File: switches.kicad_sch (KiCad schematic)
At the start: 31 parts, among them J5 BM07B-SRSS-TB, SW1 B3FS-1052, SW2 291V1022F832AB, SW3 PEC164220F-S0024, SW4 MS-22C01-G010, U4 MCP23S17_ML

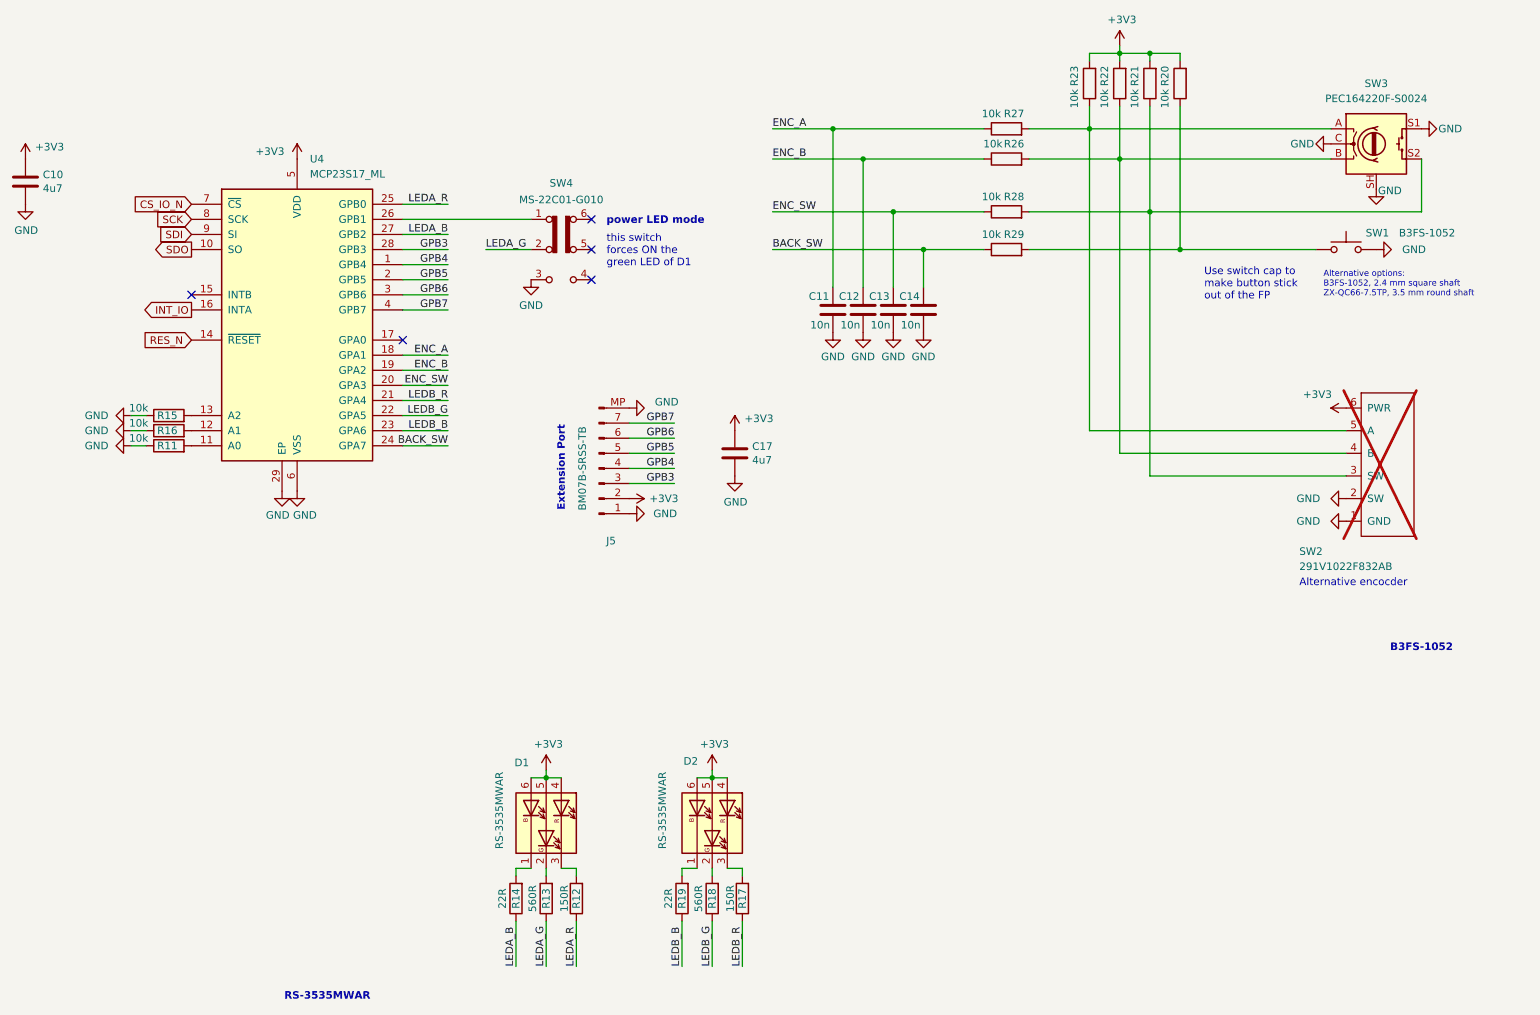
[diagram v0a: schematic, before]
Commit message: switch to 4 layers, rough routing done
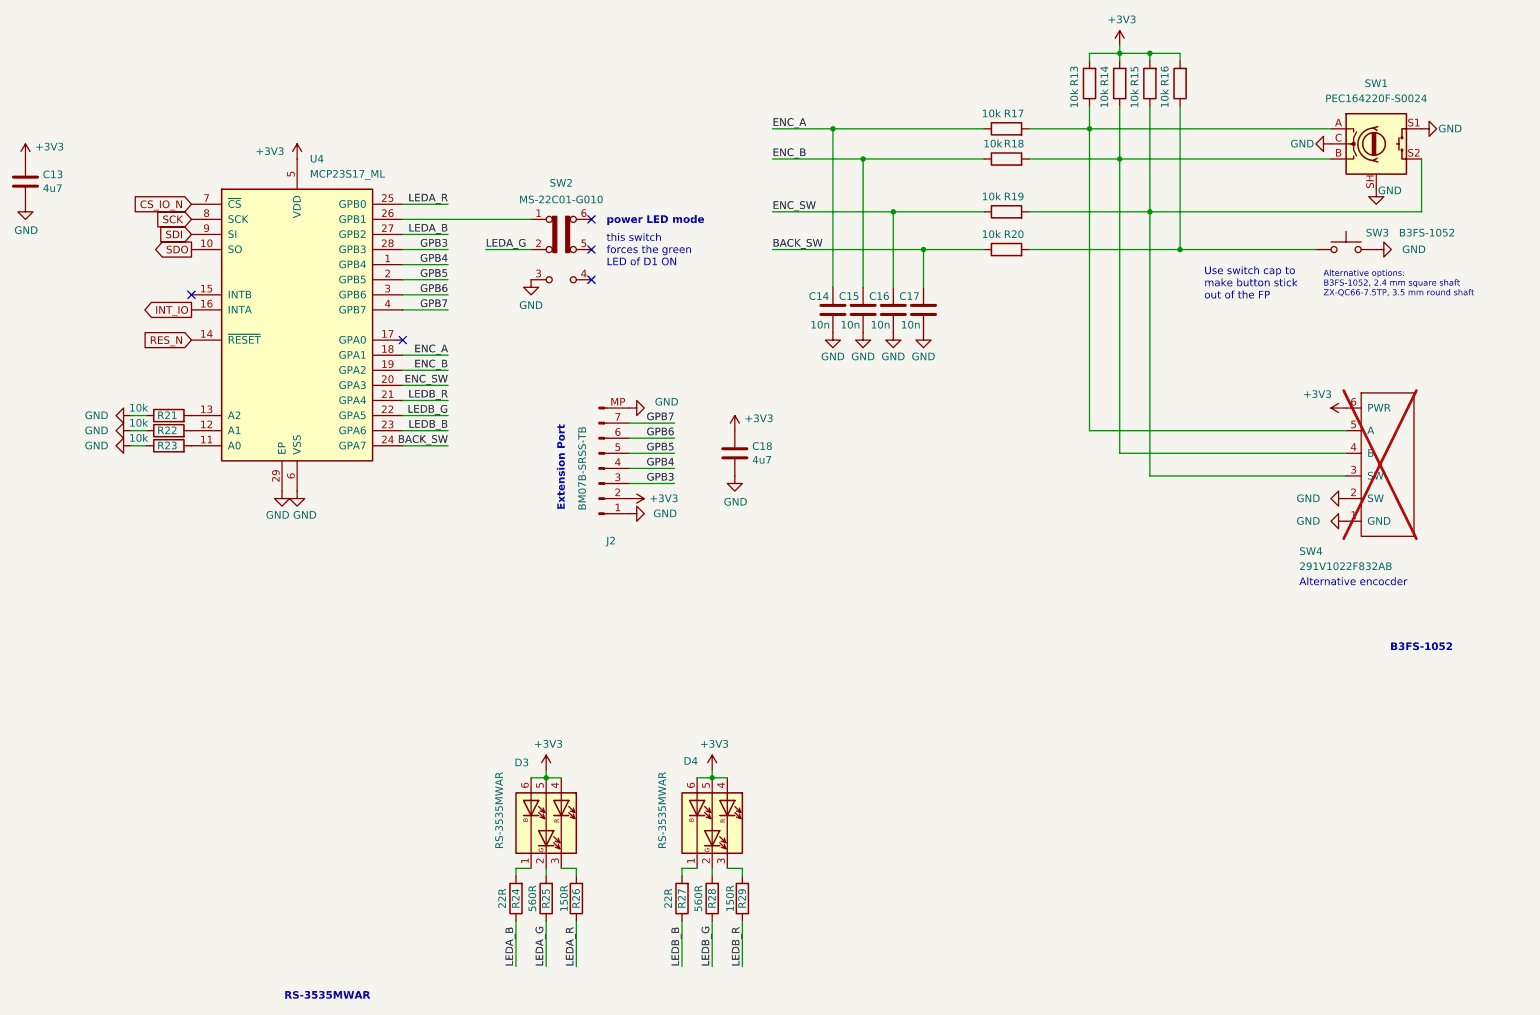
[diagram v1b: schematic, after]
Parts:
- renumbered C10 to C13, C11 to C14, C12 to C15, C13 to C16, C14 to C17, C17 to C18, D1 to D3, D2 to D4, J5 to J2, R23 to R13, R22 to R14, R21 to R15, R20 to R16, R27 to R17, R26 to R18, R28 to R19, R29 to R20, R15 to R21, R16 to R22, R11 to R23, R14 to R24, R13 to R25, R12 to R26, R19 to R27, R18 to R28, R17 to R29, SW3 to SW1, SW4 to SW2, SW1 to SW3, SW2 to SW4
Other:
- note added: "this switch forces the green LED of D1 ON"
- note removed: "this switch forces ON the green LED of D1"
